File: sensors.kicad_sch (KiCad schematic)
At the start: 14 parts, among them U2 SAM-M10Q-00B, U3 LSM6DSOX, U4 LIS2MDL, U5 LPS22DF, U7 LPS22DFTR

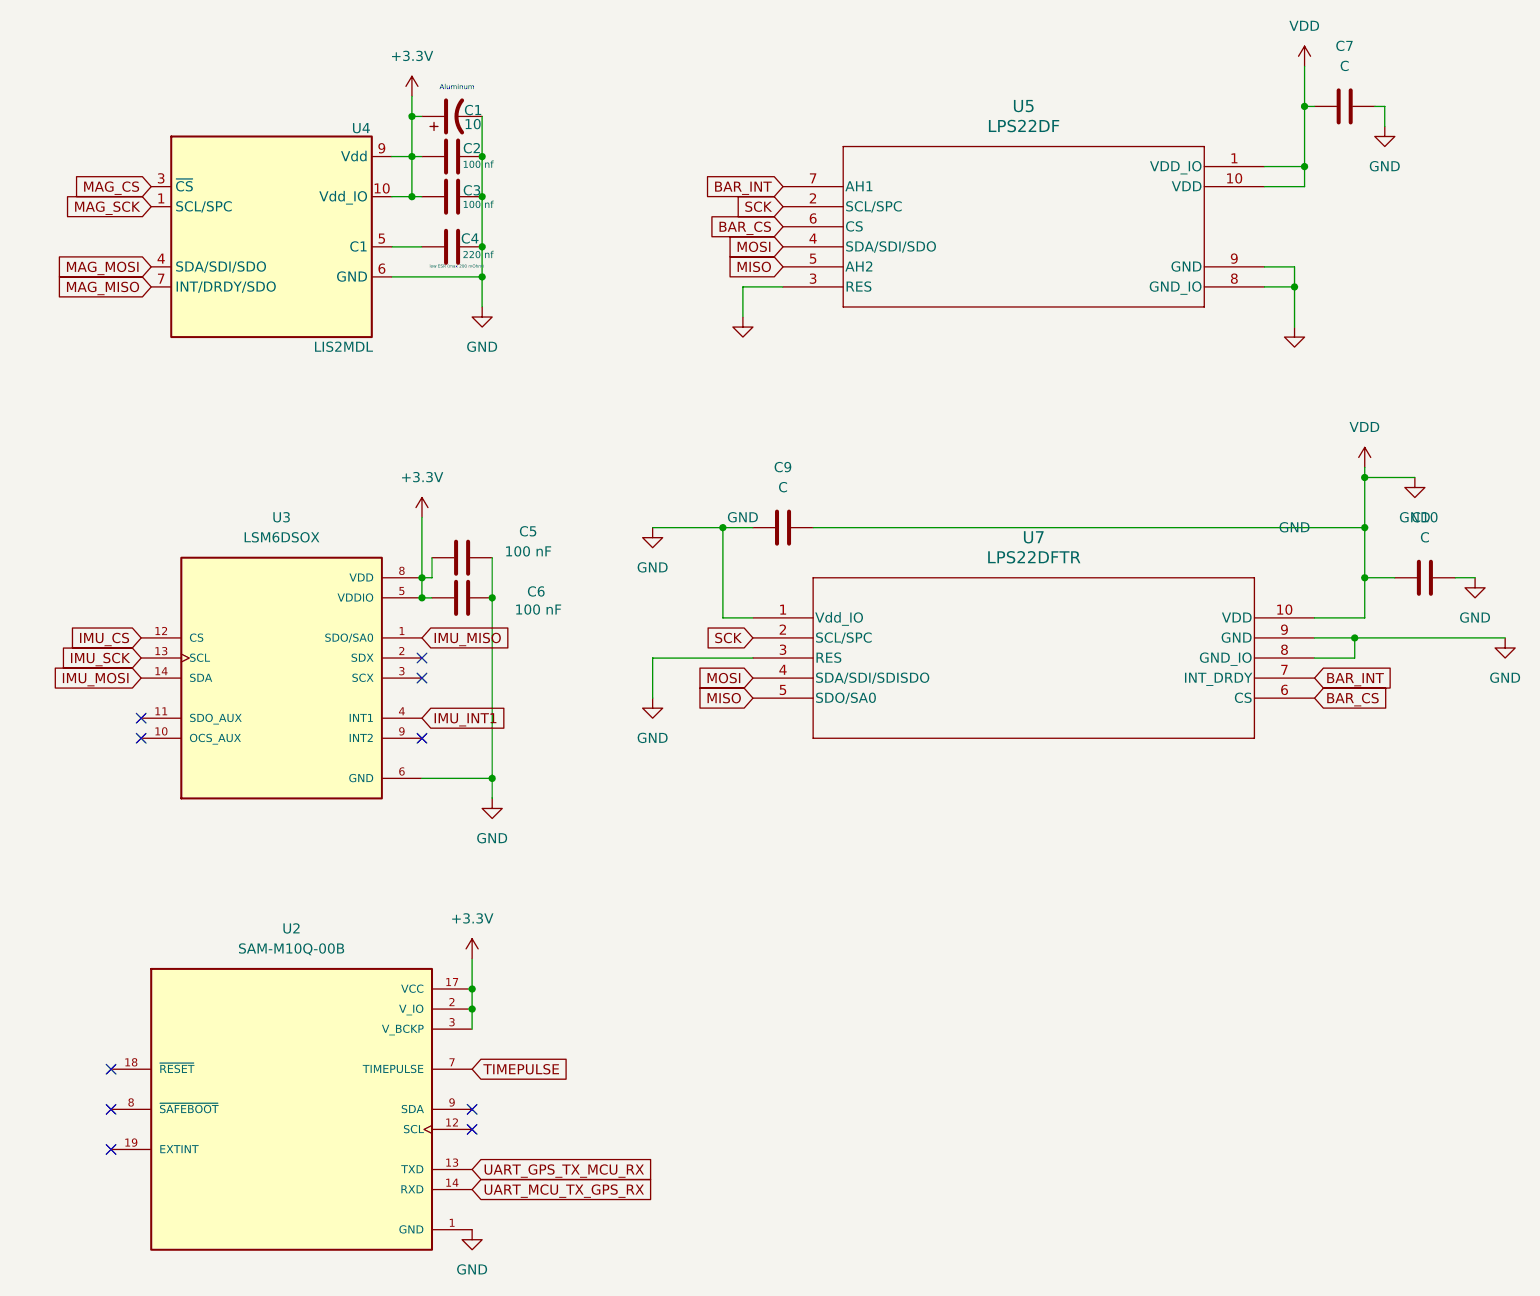
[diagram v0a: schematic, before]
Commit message: Fixed the final issues with the Barometer.
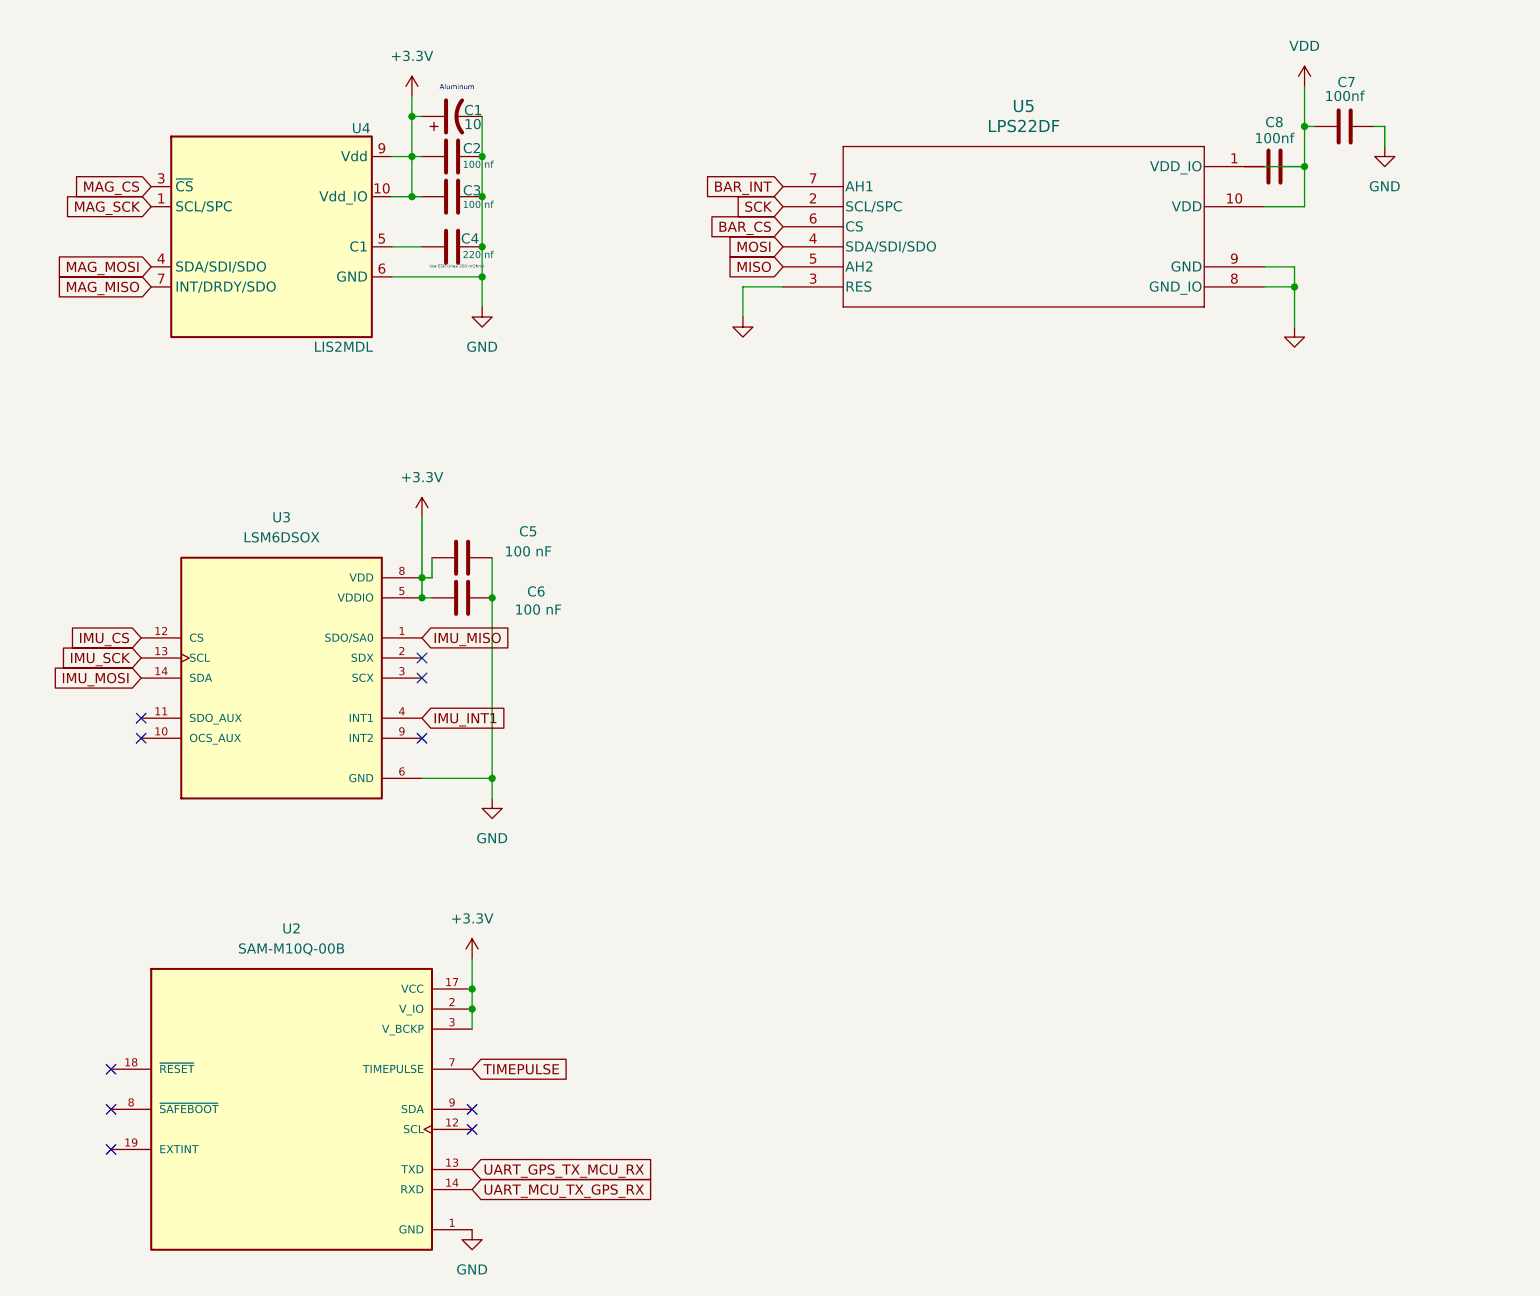
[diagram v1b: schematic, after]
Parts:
- removed C10, C9: C, Capacitor_SMD:C_0603_1608Metric, symbol Device:C
- removed U7: LPS22DFTR, QFN_22DFTR_STM, symbol New_Library:LPS22DFTR
- added C8: 100nf, Capacitor_SMD:C_0603_1608Metric, symbol Device:C
- C7: value C -> 100nf
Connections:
- net GND: no longer C7.1, U5.1 (VDD_IO), U5.10 (VDD)
- new net VDD: C7.1, C8.2, U5.1 (VDD_IO), U5.10 (VDD)
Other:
- moved on the sheet: C7

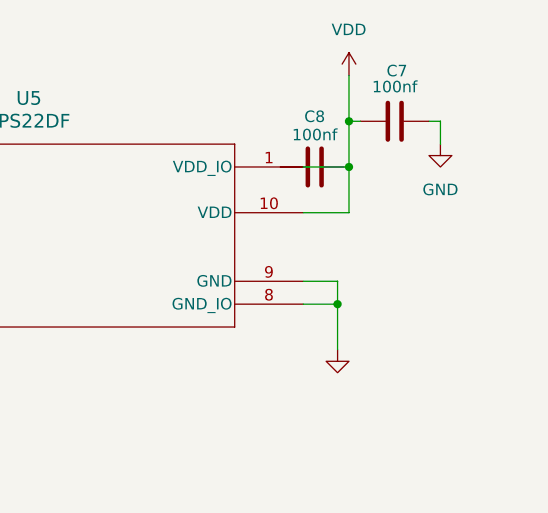
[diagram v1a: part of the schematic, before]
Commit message: Fixed the Barometer capacitors
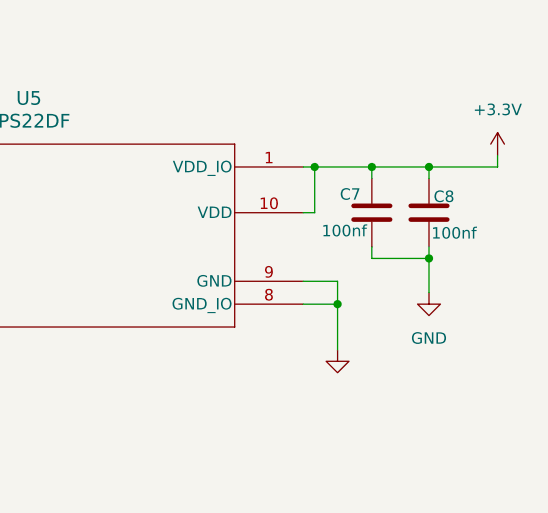
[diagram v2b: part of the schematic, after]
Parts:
- C7, C8: footprint Capacitor_SMD:C_0603_1608Metric -> (none)
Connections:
- net +3.3V: now also C7.1, C8.1, U5.1 (VDD_IO), U5.10 (VDD)
- net GND: now also C8.2
- removed net VDD: C7.1, C8.2, U5.1 (VDD_IO), U5.10 (VDD)
